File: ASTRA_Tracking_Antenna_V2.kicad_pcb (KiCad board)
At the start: 2 copper layers, 84.3 x 130.6 mm, 28 parts, among them J1 Conn_01x02_Socket, J2 24V, J3 24V, J4 24V, J5 5V, J6 Conn_01x04_Socket, M1 Stepper Motor, U2 D24V22F12, U3 DRV8846RGET, U4 D36V6F3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

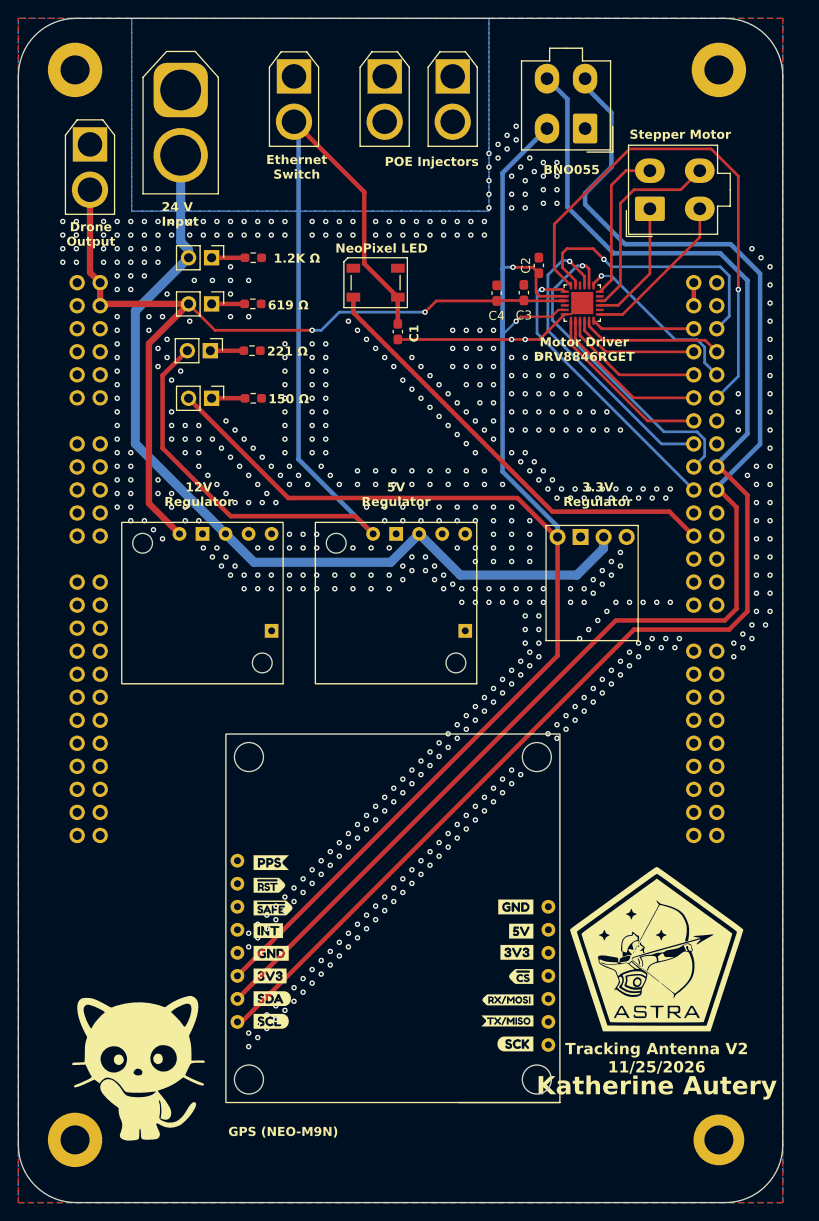
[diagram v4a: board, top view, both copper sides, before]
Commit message: Tracking Antenna V3
Tracking Antenna PCB has been revised to orient the LattePanda appropriately and replace previous power regulation system with SMD components
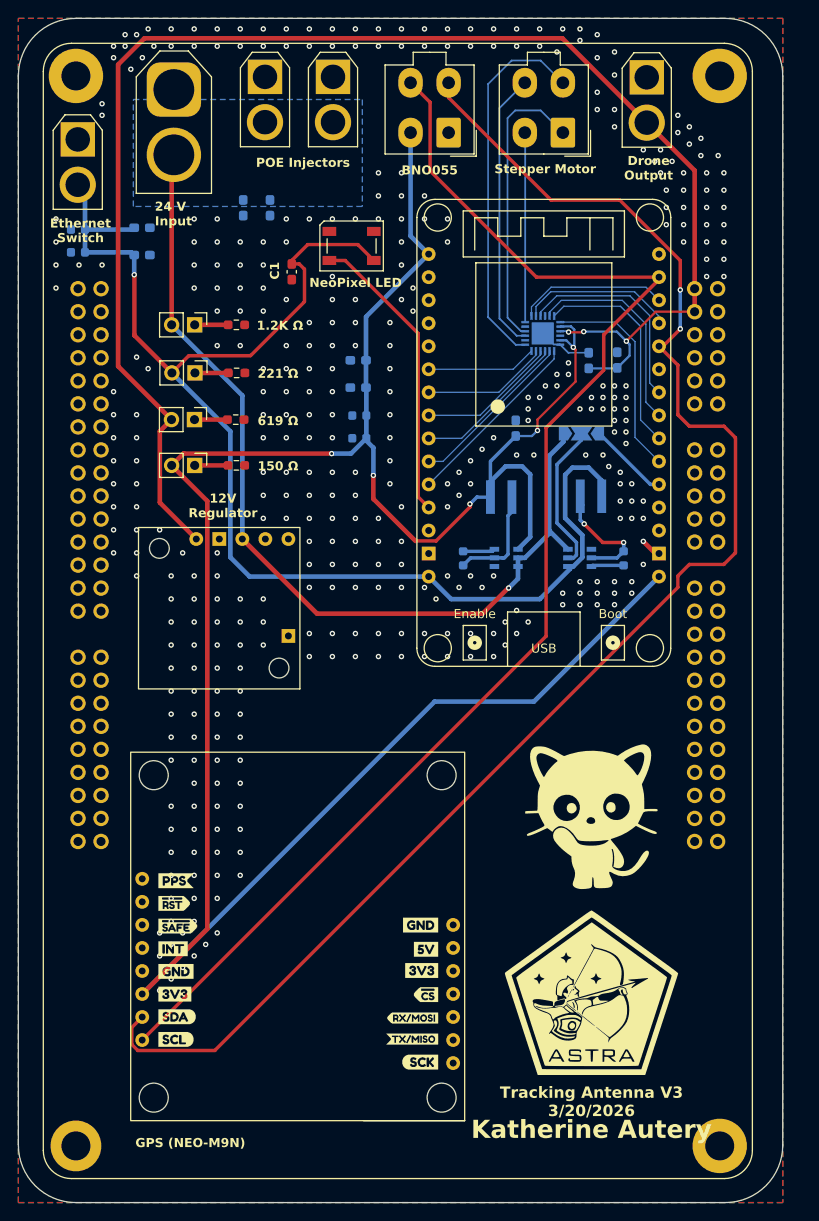
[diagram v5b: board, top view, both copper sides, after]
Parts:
- added C10: 1uF, Capacitor_SMD:C_0603_1608Metric, B.Cu at (192.2, 69.9)
- added C11: 10uF, Capacitor_SMD:C_0603_1608Metric_Pad1.08x0.95mm_HandSolder, B.Cu at (182.3, 44.5)
- added C12: 100nF, Capacitor_SMD:C_0603_1608Metric, B.Cu at (221.3, 83.2)
- added C13: 22uF, Capacitor_SMD:C_0603_1608Metric_Pad1.08x0.95mm_HandSolder, B.Cu at (168.2, 49.7)
- added C14: 22uF, Capacitor_SMD:C_0603_1608Metric_Pad1.08x0.95mm_HandSolder, B.Cu at (168.2, 46.7)
- added C15: 4u7F, Capacitor_SMD:C_0603_1608Metric, B.Cu at (161.2, 46.9)
- added C16: 1uF, Capacitor_SMD:C_0603_1608Metric, B.Cu at (161.2, 49.4)
- added C5: 10uF, Capacitor_SMD:C_0603_1608Metric_Pad1.08x0.95mm_HandSolder, B.Cu at (179.4, 44.5)
- added C6: 100nF, Capacitor_SMD:C_0603_1608Metric, B.Cu at (203.7, 83.2)
- added C7: 22uF, Capacitor_SMD:C_0603_1608Metric_Pad1.08x0.95mm_HandSolder, B.Cu at (192.1, 61.3)
- added C8: 22uF, Capacitor_SMD:C_0603_1608Metric_Pad1.08x0.95mm_HandSolder, B.Cu at (192.1, 64.3)
- added C9: 4u7F, Capacitor_SMD:C_0603_1608Metric, B.Cu at (192.2, 67.4)
- added JP1: SolderJumper_3_Open, Jumper:SolderJumper-3_P2.0mm_Open_TrianglePad1.0x1.5mm_NumberLabels, B.Cu at (216.7, 69.4)
- added L1: 4u7H, Tracking Ant:WE-MAPI_4030, B.Cu at (207.8, 76.4)
- added L2: 4u7H, Tracking Ant:WE-MAPI_4030, B.Cu at (217.8, 76.3)
- added U6: ~, Tracking Ant:esp32_devkit_v1, F.Cu at (212.6, 49.6)
- A1: moved to F.Cu
- C2, C3, C4, U3: moved to B.Cu
- U4: value D36V6F3 -> AP63203WU-7; footprint Tracking Ant:D36V6F3 3.3V -> Tracking Ant:SOT95P280X100-6N; moved to B.Cu
- U5: value D24V22F5 -> AP63205WU-7; footprint Tracking Ant:D24V22Fx -> Tracking Ant:SOT95P280X100-6N; moved to B.Cu
- moved A1 70.4 mm to (161.2, 53.4), turned to 0 degrees
- moved J1 61.8 mm to (223.9, 30.1)
- moved G*** 57.1 mm to (218.4, 111.8)
- moved J5 24.8 mm to (161.2, 37.0)
- moved C2 18.1 mm to (209.4, 68.8)
- moved U5 17.9 mm to (216.5, 83.1), turned to 0 degrees
- moved C4 15.2 mm to (220.7, 61.3)
- moved J6 15.1 mm to (202.1, 36.2)
- moved U4 13.5 mm to (208.4, 83.1)
- moved C1 13.4 mm to (184.8, 51.5)
- moved J2 13.2 mm to (189.3, 30.1)
- moved J3 13.2 mm to (181.8, 30.1)
- moved R2 12.9 mm to (178.6, 67.8)
- moved D5 12.9 mm to (174.0, 67.8)
- moved M1 12.8 mm to (214.7, 36.2), turned to 180 degrees
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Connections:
- A1 pad 10: /CurrentScalar1_Driver -> unconnected-(A1A-A3-Pad10)
- A1 pad 11: /Step_Driver -> unconnected-(A1A-D6-Pad11)
- A1 pad 12: /CurrentScalar0_Driver -> unconnected-(A1A-D13-Pad12)
- A1 pad 14: /ADEC_Driver -> unconnected-(A1A-D12-Pad14)
- A1 pad 16: /Micro1_Driver -> unconnected-(A1A-D11-Pad16)
- A1 pad 17: Sensor_SCL -> unconnected-(A1A-D3/SCL-Pad17)
- A1 pad 18: /Micro0_Driver -> unconnected-(A1A-D10-Pad18)
- A1 pad 19: Sensor_SDA -> unconnected-(A1A-D2/SDA-Pad19)
- A1 pad 20: /Dir_Driver -> unconnected-(A1A-D9-Pad20)
- A1 pad 24: /NEO_LED_DIN -> unconnected-(A1A-D7-Pad24)
- A1 pad 5: /Enable_Driver -> unconnected-(A1A-A2-Pad5)
- A1 pad 6: /Decay1_Driver -> unconnected-(A1A-A5-Pad6)
- A1 pad 7: /Sleep_Driver -> unconnected-(A1A-A1-Pad7)
- A1 pad 8: /Decay0_Driver -> unconnected-(A1A-A4-Pad8)
- A1 pad 9: /nFault_Driver -> unconnected-(A1A-A0-Pad9)
- M1 pad 1: /A2_Motor -> /B2_Motor
- M1 pad 4: /B2_Motor -> /A2_Motor
- U4 pad 1: unconnected-(U4-SHDN-Pad1) -> +3.3V
- U4 pad 3: GND -> +24V
- U4 pad 4: +3.3V -> GND
- U5 pad 1: unconnected-(U5-PG-Pad1) -> +5V
- U5 pad 2: unconnected-(U5-EN-Pad2) -> Net-(JP1-C)
- U5 pad 5: +5V -> Net-(U5-SW)
- U5 pad 6: GND -> Net-(U5-BST)
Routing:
- net +3.3V: track 181.4 -> 266.1 mm, vias 2 -> 5
- net +12V: track 96.3 -> 167.6 mm, vias 2 -> 3
- net +5V: track 115.1 -> 150.6 mm, vias 0 -> 1
- net /Step_Driver: track 57.9 -> 24.1 mm, vias 1 -> 0
- net /A1_Motor: track 17.7 -> 41.4 mm
- net /Micro0_Driver: track 36.2 -> 17.2 mm, vias 1 -> 0
- net /A2_Motor: track 14.1 -> 30.8 mm
- net /NEO_LED_DIN: track 49.4 -> 32.8 mm
- net Net-(JP1-C): track 0.00 -> 16.5 mm
- net GND: track 24.5 -> 8.23 mm, vias 655 -> 389
- net Sensor_SDA: track 151.4 -> 167.7 mm, vias 0 -> 2
- net Net-(U5-SW): track 0.00 -> 14.3 mm, vias 0 -> 2
- net Net-(U4-SW): track 0.00 -> 12.0 mm
- net /Micro1_Driver: track 33.8 -> 23.2 mm, vias 1 -> 0
- net /B2_Motor: track 22.3 -> 32.0 mm
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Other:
- board text added: "3"
- board text added: "Tracking Antenna V3 3/20/2026"
- board text removed: "3.3V Regulator"
- board text removed: "5V Regulator"
- board text removed: "Tracking Antenna V2 11/25/2026"

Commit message: Tracking Antenna V3 Revisions
Revisions made to TA PCB from recommendations. MCU switched to newer one, SMD parts shifted around, etc.
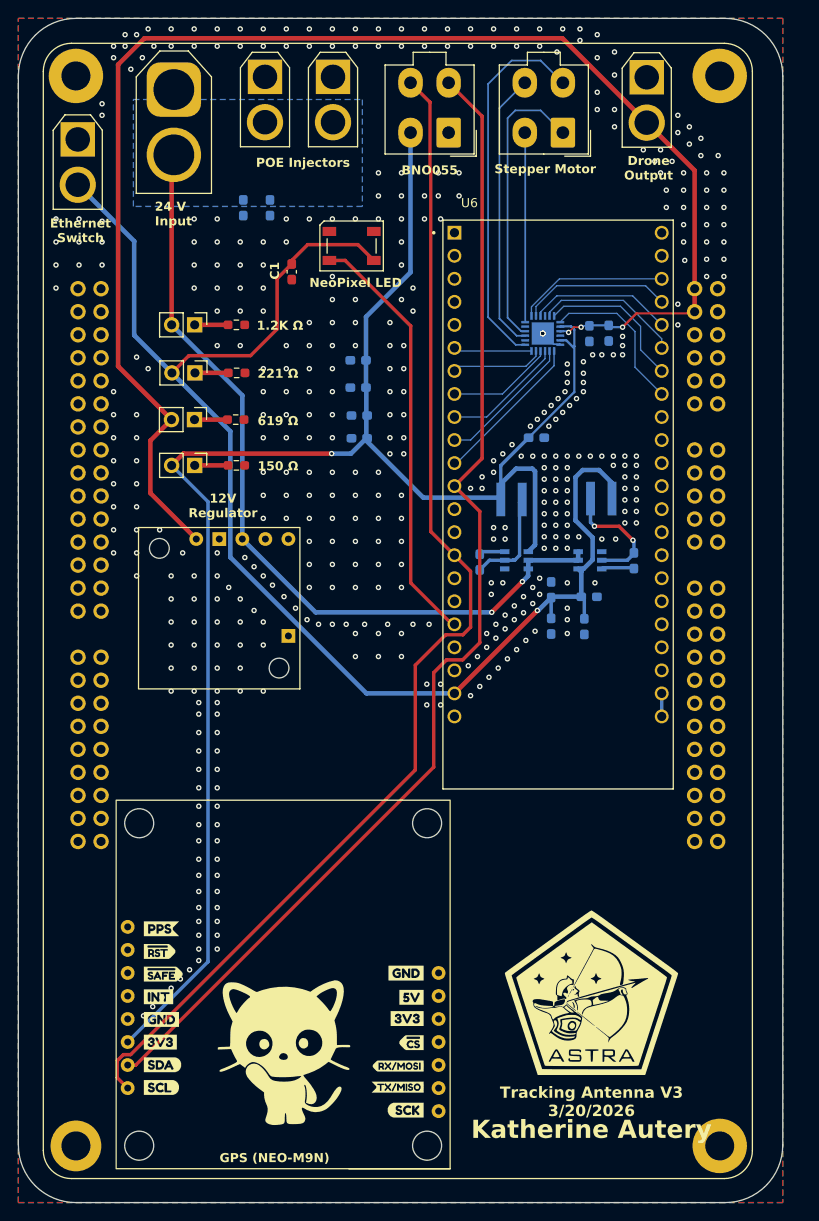
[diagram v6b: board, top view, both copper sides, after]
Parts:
- removed JP1: SolderJumper_3_Open, Jumper:SolderJumper-3_P2.0mm_Open_TrianglePad1.0x1.5mm_NumberLabels
- C10, C12, C16, C6: footprint Capacitor_SMD:C_0603_1608Metric -> Capacitor_SMD:C_0603_1608Metric_Pad1.08x0.95mm_HandSolder
- C15, C9: value 4u7F -> 4.7uF; footprint Capacitor_SMD:C_0603_1608Metric -> Capacitor_SMD:C_0603_1608Metric_Pad1.08x0.95mm_HandSolder
- U6: value ~ -> ESP32-S3-DEVKITC-1-N8R8; footprint Tracking Ant:esp32_devkit_v1 -> Tracking Ant:ESP32-S3-DEVKITC-1-N8R8
- moved C16 66.5 mm to (213.4, 90.6), turned to -90 degrees
- moved C15 65.6 mm to (213.4, 86.6), turned to 90 degrees
- moved C14 63.9 mm to (217.5, 87.4)
- moved C13 63.7 mm to (217.0, 90.7), turned to -90 degrees
- moved G*** 42.7 mm to (184.5, 137.8)
- moved U6 27.7 mm to (214.1, 77.2)
- moved U1 5.54 mm to (202.2, 109.8)
- moved C4 4.24 mm to (217.6, 58.4), turned to 90 degrees
- moved C3 3.74 mm to (219.7, 58.3), turned to 90 degrees
- moved C2 2.52 mm to (211.7, 69.8), turned to 0 degrees
- moved C6 1.88 mm to (205.5, 83.6)
- moved L2 1.17 mm to (218.9, 76.6)
- moved U5 1.17 mm to (217.6, 83.4)
- moved C12 1.17 mm to (222.5, 83.4)
- moved L1 1.17 mm to (209.0, 76.7)
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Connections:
- U5 pad 2: Net-(JP1-C) -> +24V
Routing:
- net +3.3V: track 266.1 -> 186.4 mm, vias 5 -> 1
- net Sensor_SDA: track 167.7 -> 129.9 mm, vias 2 -> 0
- net Sensor_SCL: track 148.4 -> 131.8 mm
- net Net-(JP1-C): track 16.5 -> 0.00 mm
- net /NEO_LED_DIN: track 32.8 -> 47.0 mm
- net +24V: track 104.6 -> 92.5 mm, vias 1 -> 2
- net 5VREG_EN: track 8.87 -> 0.00 mm
- net /Step_Driver: track 24.1 -> 16.8 mm
- net /Micro1_Driver: track 23.2 -> 15.9 mm
- net /Enable_Driver: track 23.4 -> 16.1 mm
- net +12V: track 167.6 -> 160.6 mm
- net /Dir_Driver: track 23.5 -> 17.6 mm
- net +5V: track 150.6 -> 156.2 mm
- net /Decay0_Driver: track 16.1 -> 11.8 mm
- net /Sleep_Driver: track 14.0 -> 10.2 mm
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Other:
- board text removed: "3"

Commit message: V3 Minor Changes
Minor part positioning changes.
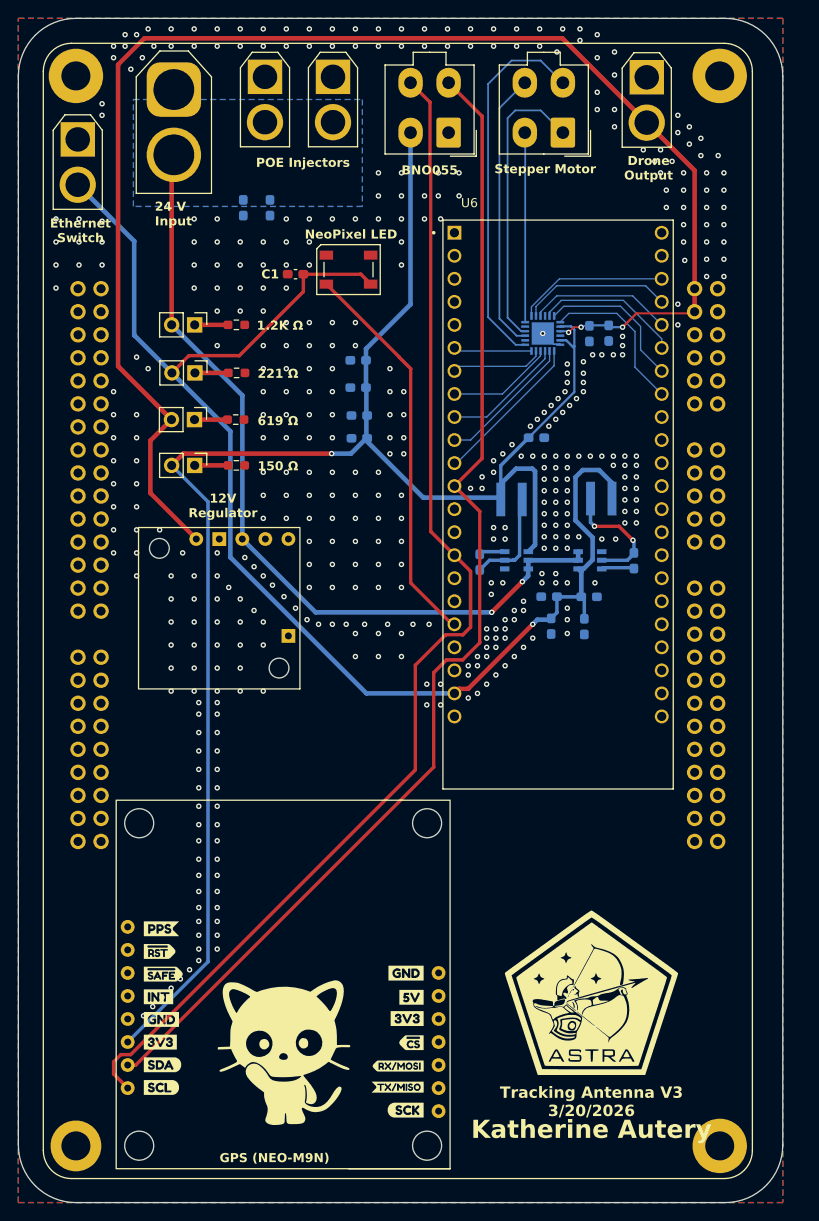
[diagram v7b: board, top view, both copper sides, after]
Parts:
- C12, C6: value 100nF -> 0.1uF
- moved D2 2.63 mm to (191.0, 51.3)
- moved C15 0.80 mm to (213.1, 87.4), turned to 180 degrees
- moved C1 0.49 mm to (185.2, 51.8), turned to 180 degrees
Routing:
- net +5V: track 156.2 -> 151.2 mm
- net /NEO_LED_DIN: track 47.0 -> 43.5 mm
- net GND: track 4.99 -> 2.45 mm, vias 454 -> 451
